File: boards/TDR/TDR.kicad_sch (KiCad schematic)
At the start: 18 parts, among them J1 USB_C_Receptacle_USB2.0, J2 SMA, U10 W25Q128JVPIQ, U14 Resistive_Power_Divider, U2 USBLC6-2SC6, U3 AxxDBF1-200.0000

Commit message: hopefully PCB is done
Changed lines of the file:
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@@
       (effects (font (size 1.27 1.27)) (justify left top))
     )
-    (pin "OUT_A" output (at 234.95 54.61 0)
+    (pin "OUT_A" output (at 234.95 59.69 0)
       (effects (font (size 1.27 1.27)) (justify right))
     )
@@
       (effects (font (size 1.27 1.27)) (justify left))
     )
-    (pin "OUT_B" output (at 234.95 59.69 0)
+    (pin "OUT_B" output (at 234.95 54.61 0)
       (effects (font (size 1.27 1.27)) (justify right))
     )
@@
       (reference "R7") (unit 1)
     )
+    (path "/00000000-0000-0000-0000-00005e56b656/f0d9aa56-55dc-4dfb-95a3-be7d7f8ba2ee"
+      (reference "TP1") (unit 1)
+    )
     (path "/00000000-0000-0000-0000-00005e56b656/00000000-0000-0000-0000-00005e7210c8"
       (reference "U1") (unit 1)
@@
       (reference "#PWR0145") (unit 1)
     )
+    (path "/f9fc04fe-099d-4539-8ef8-fc25a0dbd2d1/34930f9b-2f34-4a1c-9b41-a588d6f8c290"
+      (reference "#PWR0160") (unit 1)
+    )
+    (path "/f9fc04fe-099d-4539-8ef8-fc25a0dbd2d1/32025cef-50ea-4e1f-9cbe-56ef288a9050"
+      (reference "#PWR0161") (unit 1)
+    )
     (path "/f9fc04fe-099d-4539-8ef8-fc25a0dbd2d1/2728dc0a-4bfe-4587-8c7b-620684dd76c0"
       (reference "#PWR0186") (unit 1)
@@
       (reference "#PWR0189") (unit 1)
     )
+    (path "/f9fc04fe-099d-4539-8ef8-fc25a0dbd2d1/63729b5c-b826-418a-81a0-206377caacc5"
+      (reference "#PWR0190") (unit 1)
+    )
+    (path "/f9fc04fe-099d-4539-8ef8-fc25a0dbd2d1/b1c94a61-69ce-4634-9391-7129c54a2f7c"
+      (reference "#PWR0191") (unit 1)
+    )
     (path "/f9fc04fe-099d-4539-8ef8-fc25a0dbd2d1/00000000-0000-0000-0000-00005e86c0c5"
       (reference "C4") (unit 1)
@@
       (reference "C23") (unit 1)
     )
+    (path "/f9fc04fe-099d-4539-8ef8-fc25a0dbd2d1/3df0fc10-0822-4c59-a82f-31d1b3fd8396"
+      (reference "C27") (unit 1)
+    )
+    (path "/f9fc04fe-099d-4539-8ef8-fc25a0dbd2d1/32dffc1c-d28d-4dbb-900d-9eea11249c41"
+      (reference "C29") (unit 1)
+    )
+    (path "/f9fc04fe-099d-4539-8ef8-fc25a0dbd2d1/a7d15889-6522-4f66-8185-41360f27f8c9"
+      (reference "C31") (unit 1)
+    )
     (path "/f9fc04fe-099d-4539-8ef8-fc25a0dbd2d1/00000000-0000-0000-0000-00005ea176fb"
       (reference "FB1") (unit 1)
@@
       (reference "U15") (unit 1)
     )
+    (path "/f9fc04fe-099d-4539-8ef8-fc25a0dbd2d1/3a1ce273-62bb-48a0-a75a-c2c9c99b4ca7"
+      (reference "U16") (unit 1)
+    )
   )

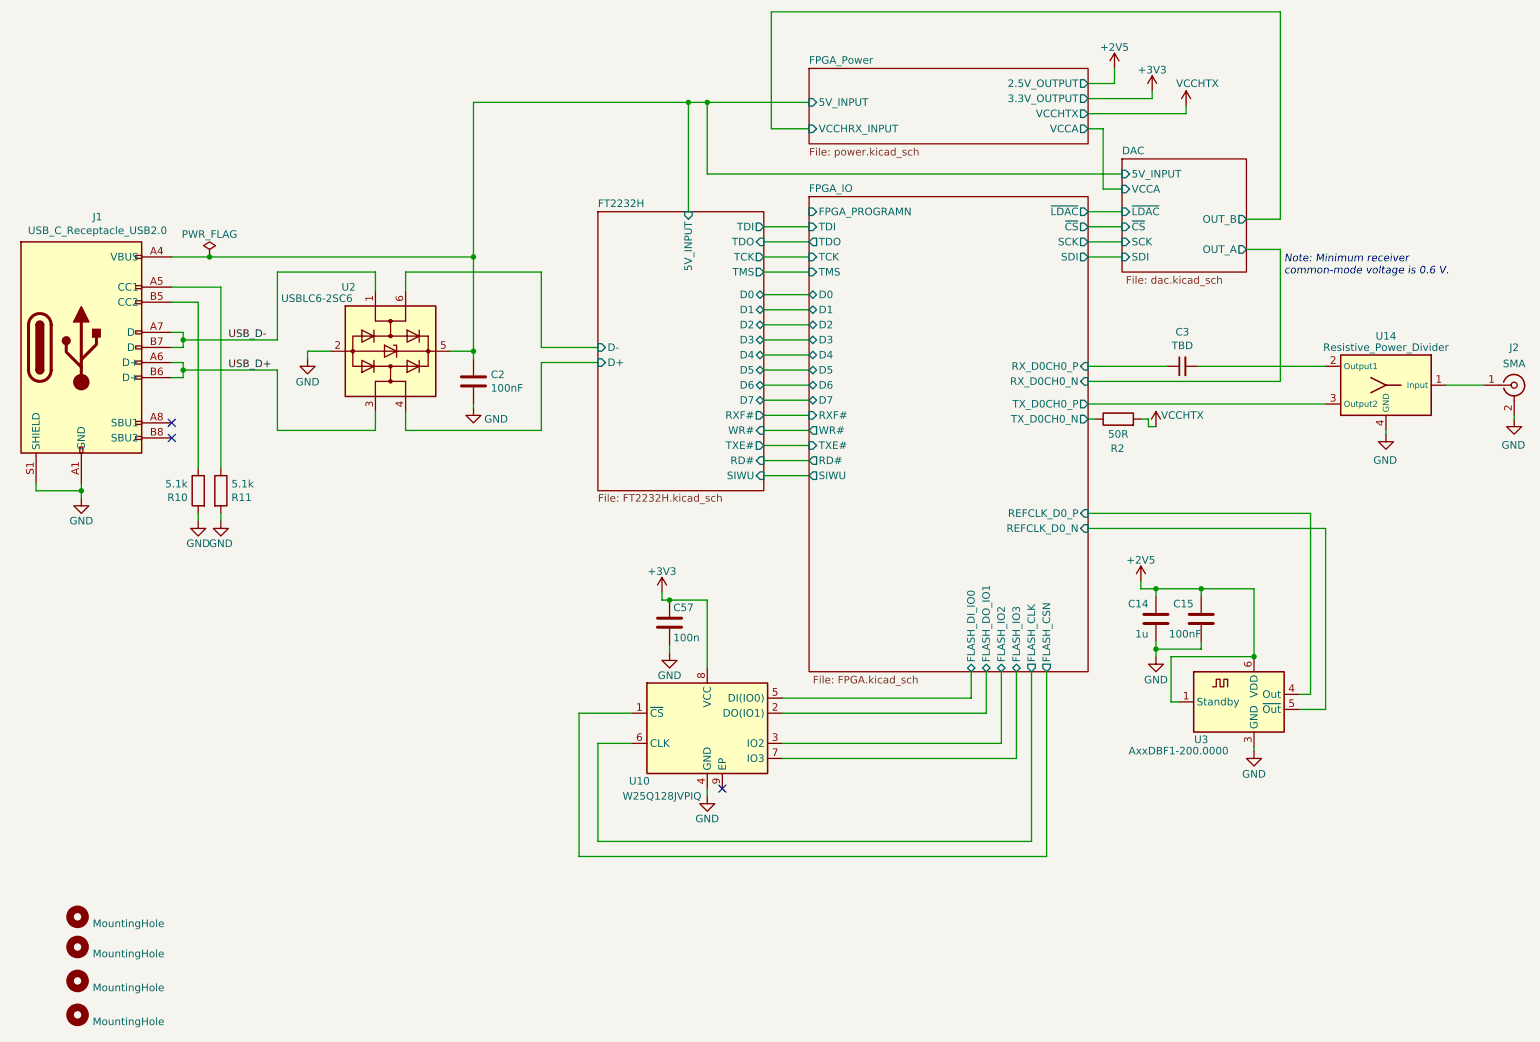
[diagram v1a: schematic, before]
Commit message: Add LD39050PUR feedback resistor values, fixed regulator enable
Fixes #1
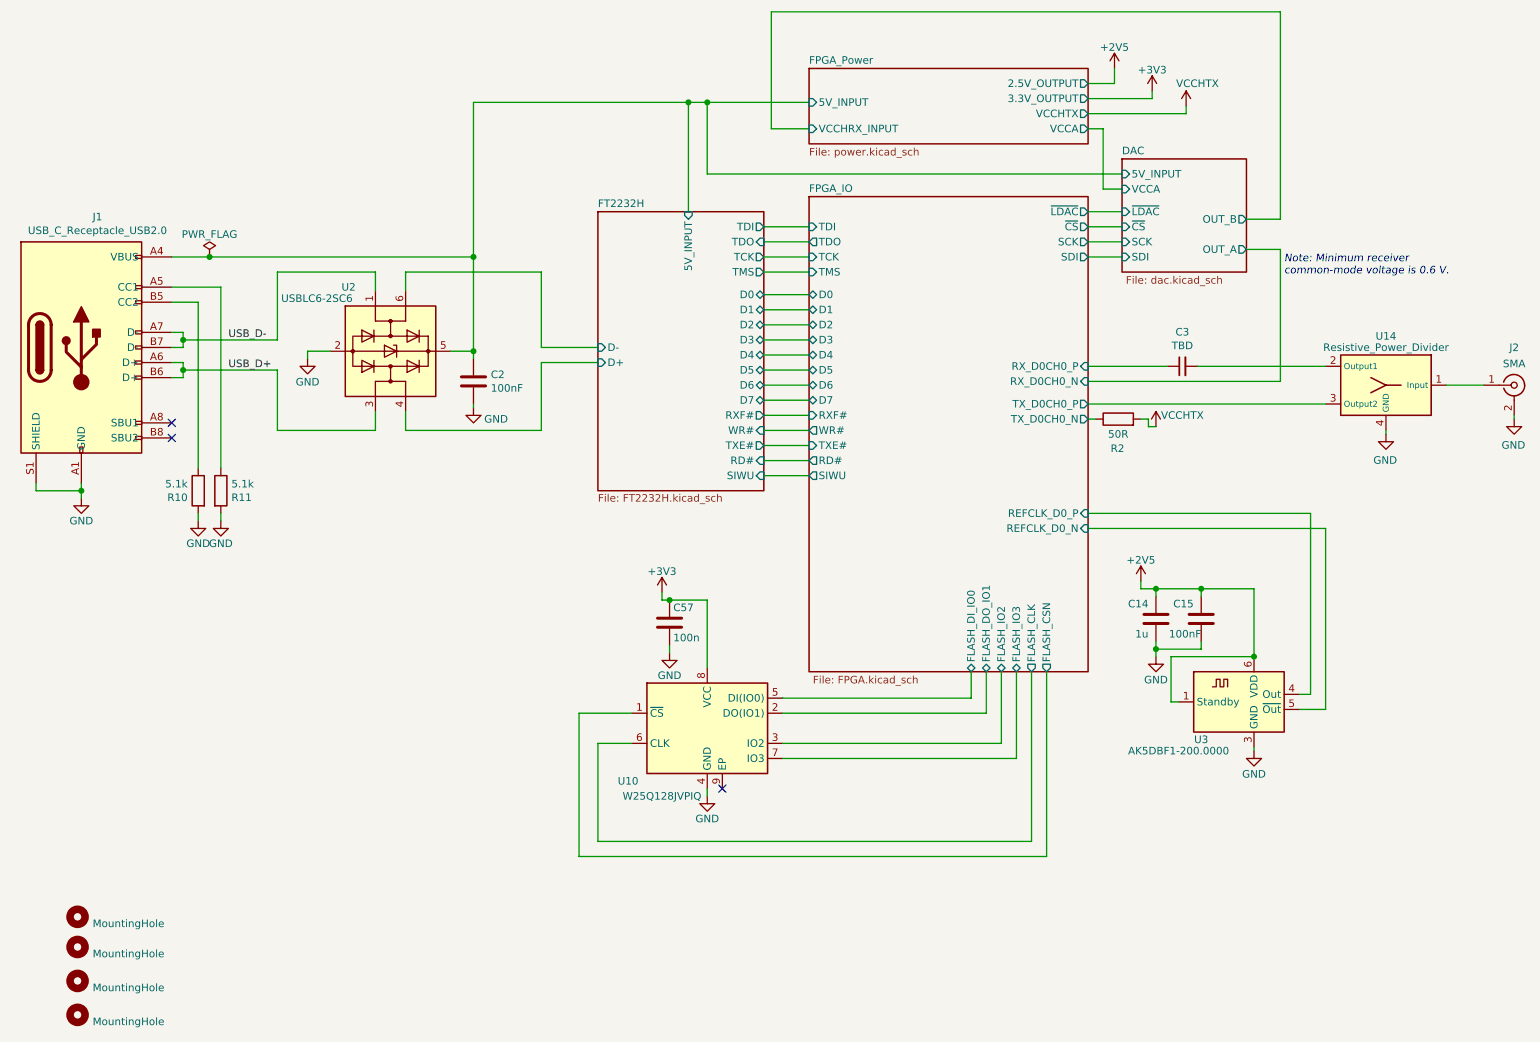
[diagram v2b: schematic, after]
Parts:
- U3: value AxxDBF1-200.0000 -> AK5DBF1-200.0000
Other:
- sheet FPGA_IO ports: added none; removed FPGA_PROGRAMN
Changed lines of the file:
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@@
-(kicad_sch (version 20200618) (host eeschema "(5.99.0-2250-gafd432e68)")
+(kicad_sch (version 20200714) (host eeschema "(5.99.0-2491-g71882a7b0)")
   (page 1 5)
   (paper "A4")
@@
     (comment 9 "9")
   )
-  (junction (at 38.735 100.33) (diameter 0) (color 0 0 0 0))
-  (junction (at 55.88 74.93) (diameter 0) (color 0 0 0 0))
-  (junction (at 55.88 80.01) (diameter 0) (color 0 0 0 0))
-  (junction (at 60.325 60.96) (diameter 0) (color 0 0 0 0))
-  (junction (at 104.775 60.96) (diameter 0) (color 0 0 0 0))
-  (junction (at 104.775 76.835) (diameter 0) (color 0 0 0 0))
-  (junction (at 137.795 118.745) (diameter 0) (color 0 0 0 0))
-  (junction (at 140.97 34.925) (diameter 0) (color 0 0 0 0))
-  (junction (at 144.145 34.925) (diameter 0) (color 0 0 0 0))
-  (junction (at 219.71 116.84) (diameter 0) (color 0 0 0 0))
-  (junction (at 219.71 127) (diameter 0) (color 0 0 0 0))
-  (junction (at 227.33 116.84) (diameter 0) (color 0 0 0 0))
-  (junction (at 236.22 128.27) (diameter 0) (color 0 0 0 0))
+  (junction (at 38.735 100.33) (diameter 1.016) (color 0 0 0 0))
+  (junction (at 55.88 74.93) (diameter 1.016) (color 0 0 0 0))
+  (junction (at 55.88 80.01) (diameter 1.016) (color 0 0 0 0))
+  (junction (at 60.325 60.96) (diameter 1.016) (color 0 0 0 0))
+  (junction (at 104.775 60.96) (diameter 1.016) (color 0 0 0 0))
+  (junction (at 104.775 76.835) (diameter 1.016) (color 0 0 0 0))
+  (junction (at 137.795 118.745) (diameter 1.016) (color 0 0 0 0))
+  (junction (at 140.97 34.925) (diameter 1.016) (color 0 0 0 0))
+  (junction (at 144.145 34.925) (diameter 1.016) (color 0 0 0 0))
+  (junction (at 219.71 116.84) (diameter 1.016) (color 0 0 0 0))
+  (junction (at 219.71 127) (diameter 1.016) (color 0 0 0 0))
+  (junction (at 227.33 116.84) (diameter 1.016) (color 0 0 0 0))
+  (junction (at 236.22 128.27) (diameter 1.016) (color 0 0 0 0))
+  (no_connect (at 53.975 88.9))
   (no_connect (at 53.975 91.44))
   (no_connect (at 146.685 150.495))
-  (no_connect (at 53.975 88.9))
   (wire (pts (xy 31.115 99.06) (xy 31.115 100.33))
     (stroke (width 0) (type solid) (color 0 0 0 0))
@@
     (in_bom yes) (on_board yes)
     (property "Reference" "U3" (id 0) (at 227.33 142.24 0))
-    (property "Value" "AxxDBF1-200.0000" (id 1) (at 223.52 144.145 0))
+    (property "Value" "AK5DBF1-200.0000" (id 1) (at 223.52 144.145 0))
     (property "Footprint" "Oscillator:Oscillator_SMD_IDT_JS6-6_5.0x3.2mm_P1.27mm" (id 2) (at 233.68 146.05 0)
       (effects (font (size 1.27 1.27)) hide)
@@
   (symbol (lib_id "Memory_Flash:W25Q32JVZP") (at 144.145 140.335 0) (unit 1)
     (in_bom yes) (on_board yes)
-    (property "Reference" "U10" (id 0) (at 132.715 149.225 0))
+    (property "Reference" "U10" (id 0) (at 130.81 149.225 0))
     (property "Value" "W25Q128JVPIQ" (id 1) (at 136.525 151.765 0))
     (property "Footprint" "Package_SON:WSON-8-1EP_6x5mm_P1.27mm_EP3.4x4.3mm" (id 2) (at 144.145 140.335 0)
@@
   )
   (sheet (at 213.995 44.45) (size 20.955 19.05)
-    (stroke (width 0.001) (type solid) (color 163 190 140 1))
+    (stroke (width 0.254) (type solid) (color 163 190 140 1))
     (fill (color 255 255 255 0.0000))
     (property "Sheet name" "DAC" (id 0) (at 213.995 43.8141 0)
@@
   )
   (sheet (at 161.29 50.8) (size 46.99 80.01)
-    (stroke (width 0.1524) (type solid) (color 163 190 140 1))
+    (stroke (width 0.254) (type solid) (color 163 190 140 1))
     (fill (color 255 255 255 0.0000))
     (property "Sheet name" "FPGA_IO" (id 0) (at 161.29 50.164 0)
@@
       (effects (font (size 1.27 1.27)) (justify left))
     )
-    (pin "FPGA_PROGRAMN" input (at 161.29 53.34 180)
-      (effects (font (size 1.27 1.27)) (justify left))
-    )
     (pin "D5" bidirectional (at 161.29 80.01 180)
       (effects (font (size 1.27 1.27)) (justify left))
@@
   )
   (sheet (at 161.29 29.21) (size 46.99 12.7)
-    (stroke (width 0.1524) (type solid) (color 163 190 140 1))
+    (stroke (width 0.254) (type solid) (color 163 190 140 1))
     (fill (color 255 255 255 0.0000))
     (property "Sheet name" "FPGA_Power" (id 0) (at 161.29 28.5745 0)
@@
   )
   (sheet (at 125.73 53.34) (size 27.94 46.99)
-    (stroke (width 0.1524) (type solid) (color 163 190 140 1))
+    (stroke (width 0.254) (type solid) (color 163 190 140 1))
     (fill (color 255 255 255 0.0000))
     (property "Sheet name" "FT2232H" (id 0) (at 125.73 52.7045 0)
@@
       (reference "TP1") (unit 1)
     )
-    (path "/00000000-0000-0000-0000-00005e56b656/00000000-0000-0000-0000-00005e7210c8"
-      (reference "U1") (unit 1)
-    )
-    (path "/00000000-0000-0000-0000-00005e56b656/00000000-0000-0000-0000-00005e7210d4"
-      (reference "U1") (unit 2)
-    )
     (path "/00000000-0000-0000-0000-00005e56b656/00000000-0000-0000-0000-00005e7210e0"
       (reference "U1") (unit 3)
     )
-    (path "/00000000-0000-0000-0000-00005e56b656/00000000-0000-0000-0000-00005e7210f8"
-      (reference "U1") (unit 4)
-    )
     (path "/00000000-0000-0000-0000-00005e56b656/00000000-0000-0000-0000-00005e721098"
       (reference "U1") (unit 5)
@@
       (reference "U1") (unit 6)
     )
-    (path "/00000000-0000-0000-0000-00005e56b656/00000000-0000-0000-0000-00005e7210b0"
-      (reference "U1") (unit 7)
-    )
-    (path "/00000000-0000-0000-0000-00005e56b656/00000000-0000-0000-0000-00005e721104"
-      (reference "U1") (unit 8)
-    )
     (path "/00000000-0000-0000-0000-00005e56b656/00000000-0000-0000-0000-00005e7210ec"
       (reference "U1") (unit 9)
@@
       (reference "U1") (unit 10)
     )
-    (path "/00000000-0000-0000-0000-00005e56b656/00000000-0000-0000-0000-00005e72108c"
-      (reference "U1") (unit 11)
-    )
     (path "/f9fc04fe-099d-4539-8ef8-fc25a0dbd2d1/00000000-0000-0000-0000-00005e876c98"
